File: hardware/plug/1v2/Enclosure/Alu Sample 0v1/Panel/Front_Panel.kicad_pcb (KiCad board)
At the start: 2 copper layers, 65.8 x 42.7 mm, 11 parts

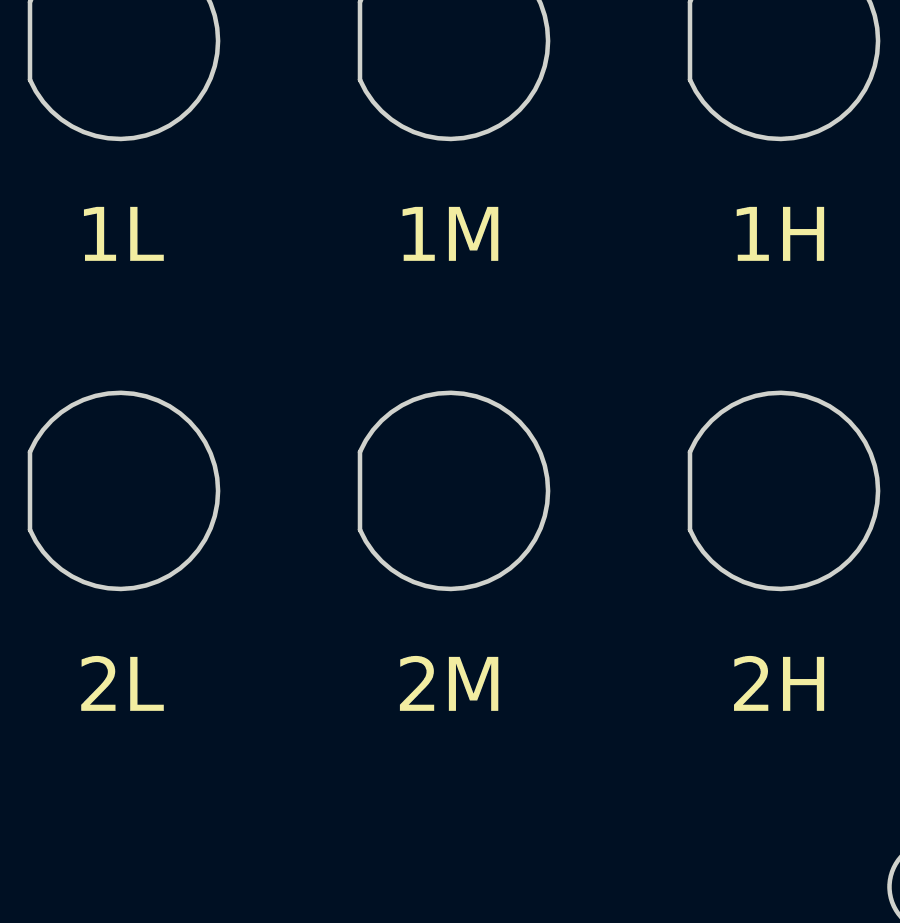
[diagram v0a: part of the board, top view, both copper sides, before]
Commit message: Low, High, Wide - TX
fix
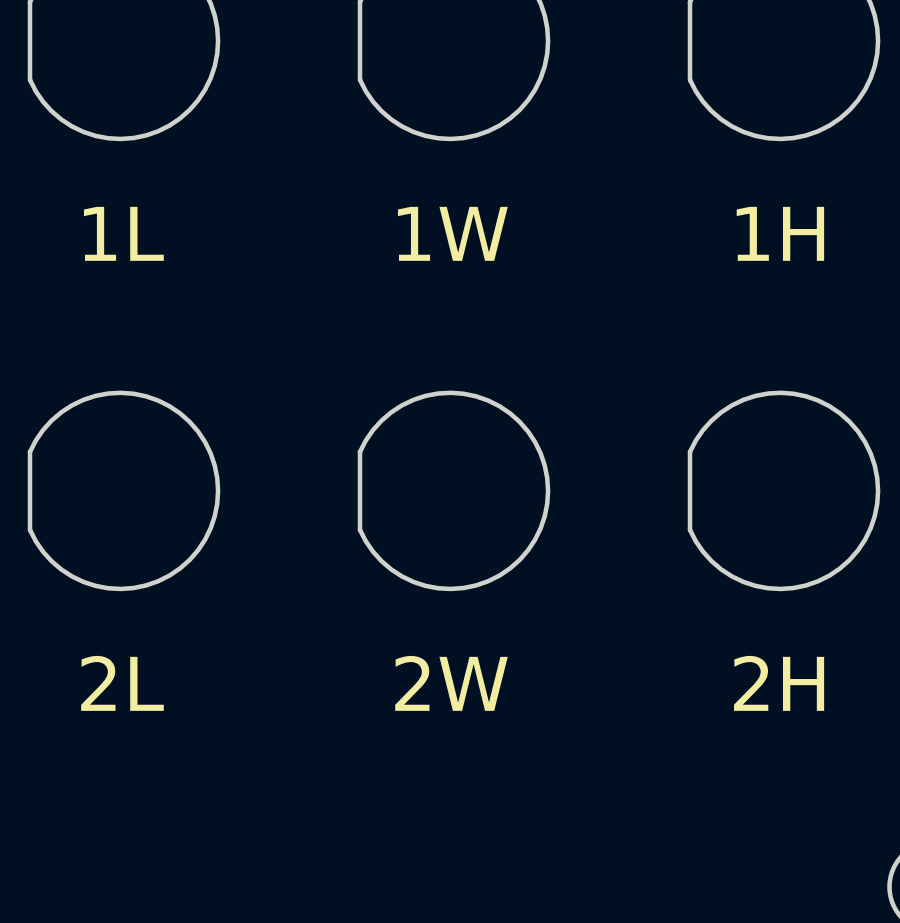
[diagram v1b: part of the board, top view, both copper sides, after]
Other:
- board text added: "1W"
- board text added: "2W"
- board text removed: "1M"
- board text removed: "2M"
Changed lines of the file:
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@@
     (links 0)
     (no_connects 0)
-    (area 100.874999 38.724999 166.825001 81.575001)
+    (area 98.532143 38.524999 167.025001 87.4925)
     (thickness 1.6)
     (drawings 28)
@@
     (pad_to_mask_clearance 0.2)
     (aux_axis_origin 0 0)
-    (visible_elements FFFFFF7F)
+    (visible_elements 7FFFFFFF)
     (pcbplotparams
       (layerselection 0x00030_ffffffff)
@@
     (effects (font (size 1.8 1.8) (thickness 0.4)))
   )
-  (gr_text 2M (at 146.6 71.2) (layer F.SilkS)
+  (gr_text 2W (at 146.6 71.2) (layer F.SilkS)
     (effects (font (size 1.8 1.8) (thickness 0.4)))
   )
@@
     (effects (font (size 1.8 1.8) (thickness 0.4)))
   )
-  (gr_text 1M (at 146.6 56.2) (layer F.SilkS)
+  (gr_text 1W (at 146.6 56.2) (layer F.SilkS)
     (effects (font (size 1.8 1.8) (thickness 0.4)))
   )
